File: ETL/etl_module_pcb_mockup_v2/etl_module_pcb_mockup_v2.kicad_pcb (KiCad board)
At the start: 2 copper layers, 43.1 x 56.5 mm, 10 parts, among them J1 WP7B-S050VA1-R8000, J2 WP7B-S050VA1-R8000, J3 ETROC_91pad, J4 ETROC_91pad, J5 ETROC_91pad, J6 ETROC_91pad

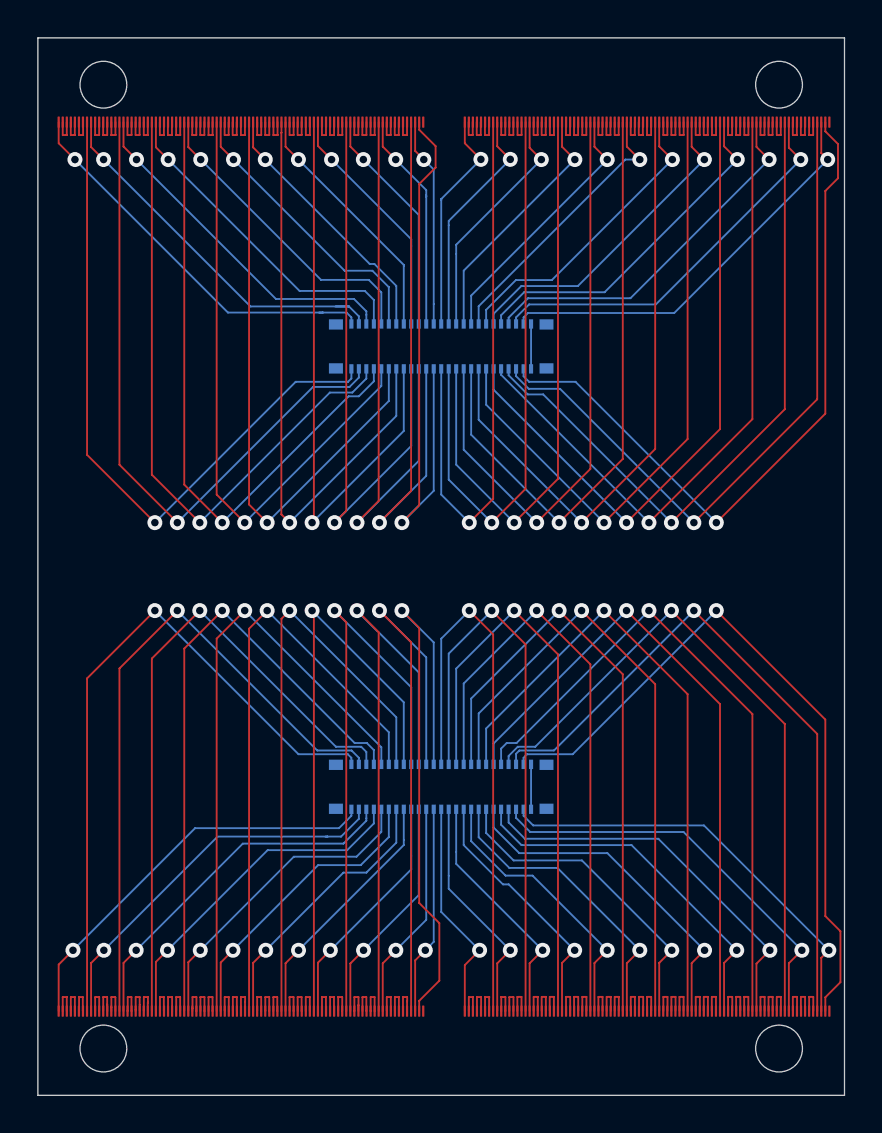
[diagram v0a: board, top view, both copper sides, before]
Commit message: Adds mockups for throughput testing
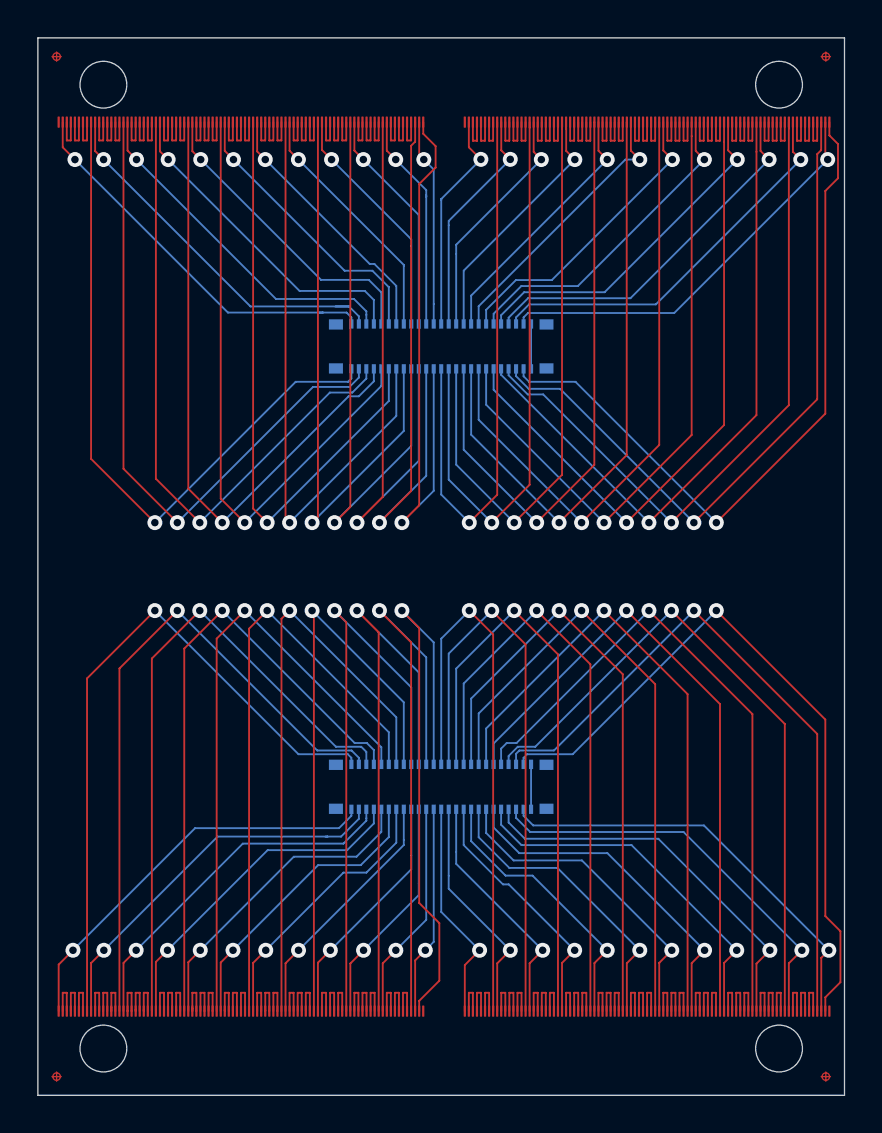
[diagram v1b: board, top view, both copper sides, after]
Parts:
- added REF**: crossed_circle_fiducial, unl_silab:crossed_circle_fiducial, F.Cu at (42.1, 55.5)
- added REF**: crossed_circle_fiducial, unl_silab:crossed_circle_fiducial, F.Cu at (1.00, 55.5)
- added REF**: crossed_circle_fiducial, unl_silab:crossed_circle_fiducial, F.Cu at (42.1, 1.00)
- added REF**: crossed_circle_fiducial, unl_silab:crossed_circle_fiducial, F.Cu at (1.00, 1.00)
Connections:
- J3 pad 1: /26_P -> Net-(J3-Pad1)
- J3 pad 10: Net-(J3-Pad10) -> /27_P
- J3 pad 11: Net-(J3-Pad10) -> Net-(J3-Pad11)
- J3 pad 12: Net-(J3-Pad12) -> Net-(J3-Pad11)
- J3 pad 13: Net-(J3-Pad12) -> Net-(J3-Pad13)
- J3 pad 14: Net-(J3-Pad14) -> Net-(J3-Pad13)
- J3 pad 15: Net-(J3-Pad14) -> Net-(J3-Pad15)
- J3 pad 16: /27_N -> Net-(J3-Pad15)
- J3 pad 17: /28_P -> /27_N
- J3 pad 18: Net-(J3-Pad18) -> /28_P
- J3 pad 19: Net-(J3-Pad18) -> Net-(J3-Pad19)
- J3 pad 2: Net-(J3-Pad2) -> /26_P
- J3 pad 20: Net-(J3-Pad20) -> Net-(J3-Pad19)
- J3 pad 21: Net-(J3-Pad20) -> Net-(J3-Pad21)
- J3 pad 22: Net-(J3-Pad22) -> Net-(J3-Pad21)
- J3 pad 23: Net-(J3-Pad22) -> Net-(J3-Pad23)
- J3 pad 24: /28_N -> Net-(J3-Pad23)
- J3 pad 25: /29_P -> /28_N
- J3 pad 26: Net-(J3-Pad26) -> /29_P
- J3 pad 27: Net-(J3-Pad26) -> Net-(J3-Pad27)
- J3 pad 28: Net-(J3-Pad28) -> Net-(J3-Pad27)
- J3 pad 29: Net-(J3-Pad28) -> Net-(J3-Pad29)
- J3 pad 3: Net-(J3-Pad2) -> Net-(J3-Pad3)
- J3 pad 30: Net-(J3-Pad30) -> Net-(J3-Pad29)
- J3 pad 31: Net-(J3-Pad30) -> Net-(J3-Pad31)
- J3 pad 32: /29_N -> Net-(J3-Pad31)
- J3 pad 33: /30_P -> /29_N
- J3 pad 34: Net-(J3-Pad34) -> /30_P
- J3 pad 35: Net-(J3-Pad34) -> Net-(J3-Pad35)
- J3 pad 36: Net-(J3-Pad36) -> Net-(J3-Pad35)
- J3 pad 37: Net-(J3-Pad36) -> Net-(J3-Pad37)
- J3 pad 38: Net-(J3-Pad38) -> Net-(J3-Pad37)
- J3 pad 39: Net-(J3-Pad38) -> Net-(J3-Pad39)
- J3 pad 4: Net-(J3-Pad4) -> Net-(J3-Pad3)
- J3 pad 40: /30_N -> Net-(J3-Pad39)
- J3 pad 41: /31_P -> /30_N
- J3 pad 42: Net-(J3-Pad42) -> /31_P
- J3 pad 43: Net-(J3-Pad42) -> Net-(J3-Pad43)
- J3 pad 44: Net-(J3-Pad44) -> Net-(J3-Pad43)
- J3 pad 45: Net-(J3-Pad44) -> Net-(J3-Pad45)
- J3 pad 46: Net-(J3-Pad46) -> Net-(J3-Pad45)
- J3 pad 47: Net-(J3-Pad46) -> Net-(J3-Pad47)
- J3 pad 48: /31_N -> Net-(J3-Pad47)
- J3 pad 49: /32_P -> /31_N
- J3 pad 5: Net-(J3-Pad4) -> Net-(J3-Pad5)
- J3 pad 50: Net-(J3-Pad50) -> /32_P
- J3 pad 51: Net-(J3-Pad50) -> Net-(J3-Pad51)
- J3 pad 52: Net-(J3-Pad52) -> Net-(J3-Pad51)
- J3 pad 53: Net-(J3-Pad52) -> Net-(J3-Pad53)
- J3 pad 54: Net-(J3-Pad54) -> Net-(J3-Pad53)
- J3 pad 55: Net-(J3-Pad54) -> Net-(J3-Pad55)
- J3 pad 56: /32_N -> Net-(J3-Pad55)
- J3 pad 57: /33_P -> /32_N
- J3 pad 58: Net-(J3-Pad58) -> /33_P
- J3 pad 59: Net-(J3-Pad58) -> Net-(J3-Pad59)
- J3 pad 6: Net-(J3-Pad6) -> Net-(J3-Pad5)
- J3 pad 60: Net-(J3-Pad60) -> Net-(J3-Pad59)
- J3 pad 61: Net-(J3-Pad60) -> Net-(J3-Pad61)
- J3 pad 62: Net-(J3-Pad62) -> Net-(J3-Pad61)
- J3 pad 63: Net-(J3-Pad62) -> Net-(J3-Pad63)
- J3 pad 64: /33_N -> Net-(J3-Pad63)
- J3 pad 65: /34_P -> /33_N
- J3 pad 66: Net-(J3-Pad66) -> /34_P
- J3 pad 67: Net-(J3-Pad66) -> Net-(J3-Pad67)
- J3 pad 68: Net-(J3-Pad68) -> Net-(J3-Pad67)
- J3 pad 69: Net-(J3-Pad68) -> Net-(J3-Pad69)
- J3 pad 7: Net-(J3-Pad6) -> Net-(J3-Pad7)
- J3 pad 70: Net-(J3-Pad70) -> Net-(J3-Pad69)
- J3 pad 71: Net-(J3-Pad70) -> Net-(J3-Pad71)
- J3 pad 72: /34_N -> Net-(J3-Pad71)
- J3 pad 73: /35_P -> /34_N
- J3 pad 74: Net-(J3-Pad74) -> /35_P
- J3 pad 75: Net-(J3-Pad74) -> Net-(J3-Pad75)
- J3 pad 76: Net-(J3-Pad76) -> Net-(J3-Pad75)
- J3 pad 77: Net-(J3-Pad76) -> Net-(J3-Pad77)
- J3 pad 78: Net-(J3-Pad78) -> Net-(J3-Pad77)
- J3 pad 79: Net-(J3-Pad78) -> Net-(J3-Pad79)
- J3 pad 8: /26_N -> Net-(J3-Pad7)
- J3 pad 80: /35_N -> Net-(J3-Pad79)
- J3 pad 81: /36_P -> /35_N
- J3 pad 82: Net-(J3-Pad82) -> /36_P
- J3 pad 83: Net-(J3-Pad82) -> Net-(J3-Pad83)
- J3 pad 84: Net-(J3-Pad84) -> Net-(J3-Pad83)
- J3 pad 85: Net-(J3-Pad84) -> Net-(J3-Pad85)
- J3 pad 86: Net-(J3-Pad86) -> Net-(J3-Pad85)
- J3 pad 87: Net-(J3-Pad86) -> Net-(J3-Pad87)
- J3 pad 88: /36_N -> Net-(J3-Pad87)
- J3 pad 89: /37_P -> /36_N
- J3 pad 9: /27_P -> /26_N
- J3 pad 90: /37_N -> /37_P
- J3 pad 91: Net-(J3-Pad91) -> /37_N
- J4 pad 1: /38_P -> Net-(J4-Pad1)
- J4 pad 10: Net-(J4-Pad10) -> /39_P
- J4 pad 11: Net-(J4-Pad10) -> Net-(J4-Pad11)
- J4 pad 12: Net-(J4-Pad12) -> Net-(J4-Pad11)
- J4 pad 13: Net-(J4-Pad12) -> Net-(J4-Pad13)
- J4 pad 14: Net-(J4-Pad14) -> Net-(J4-Pad13)
- J4 pad 15: Net-(J4-Pad14) -> Net-(J4-Pad15)
- J4 pad 16: /39_N -> Net-(J4-Pad15)
- J4 pad 17: /40_P -> /39_N
- J4 pad 18: Net-(J4-Pad18) -> /40_P
- J4 pad 19: Net-(J4-Pad18) -> Net-(J4-Pad19)
- J4 pad 2: Net-(J4-Pad2) -> /38_P
- J4 pad 20: Net-(J4-Pad20) -> Net-(J4-Pad19)
- J4 pad 21: Net-(J4-Pad20) -> Net-(J4-Pad21)
- J4 pad 22: Net-(J4-Pad22) -> Net-(J4-Pad21)
- J4 pad 23: Net-(J4-Pad22) -> Net-(J4-Pad23)
- J4 pad 24: /40_N -> Net-(J4-Pad23)
- J4 pad 25: /41_P -> /40_N
- J4 pad 26: Net-(J4-Pad26) -> /41_P
- J4 pad 27: Net-(J4-Pad26) -> Net-(J4-Pad27)
- J4 pad 28: Net-(J4-Pad28) -> Net-(J4-Pad27)
- J4 pad 29: Net-(J4-Pad28) -> Net-(J4-Pad29)
- J4 pad 3: Net-(J4-Pad2) -> Net-(J4-Pad3)
- J4 pad 30: Net-(J4-Pad30) -> Net-(J4-Pad29)
- J4 pad 31: Net-(J4-Pad30) -> Net-(J4-Pad31)
- J4 pad 32: /41_N -> Net-(J4-Pad31)
- J4 pad 33: /42_P -> /41_N
- J4 pad 34: Net-(J4-Pad34) -> /42_P
- J4 pad 35: Net-(J4-Pad34) -> Net-(J4-Pad35)
- J4 pad 36: Net-(J4-Pad36) -> Net-(J4-Pad35)
- J4 pad 37: Net-(J4-Pad36) -> Net-(J4-Pad37)
- J4 pad 38: Net-(J4-Pad38) -> Net-(J4-Pad37)
- J4 pad 39: Net-(J4-Pad38) -> Net-(J4-Pad39)
- J4 pad 4: Net-(J4-Pad4) -> Net-(J4-Pad3)
- J4 pad 40: /42_N -> Net-(J4-Pad39)
- J4 pad 41: /43_P -> /42_N
- J4 pad 42: Net-(J4-Pad42) -> /43_P
- J4 pad 43: Net-(J4-Pad42) -> Net-(J4-Pad43)
- J4 pad 44: Net-(J4-Pad44) -> Net-(J4-Pad43)
- J4 pad 45: Net-(J4-Pad44) -> Net-(J4-Pad45)
- J4 pad 46: Net-(J4-Pad46) -> Net-(J4-Pad45)
- J4 pad 47: Net-(J4-Pad46) -> Net-(J4-Pad47)
- J4 pad 48: /43_N -> Net-(J4-Pad47)
- J4 pad 49: /44_P -> /43_N
- J4 pad 5: Net-(J4-Pad4) -> Net-(J4-Pad5)
- J4 pad 50: Net-(J4-Pad50) -> /44_P
- J4 pad 51: Net-(J4-Pad50) -> Net-(J4-Pad51)
- J4 pad 52: Net-(J4-Pad52) -> Net-(J4-Pad51)
- J4 pad 53: Net-(J4-Pad52) -> Net-(J4-Pad53)
- J4 pad 54: Net-(J4-Pad54) -> Net-(J4-Pad53)
- J4 pad 55: Net-(J4-Pad54) -> Net-(J4-Pad55)
- J4 pad 56: /44_N -> Net-(J4-Pad55)
- J4 pad 57: /45_P -> /44_N
- J4 pad 58: Net-(J4-Pad58) -> /45_P
- J4 pad 59: Net-(J4-Pad58) -> Net-(J4-Pad59)
- J4 pad 6: Net-(J4-Pad6) -> Net-(J4-Pad5)
- J4 pad 60: Net-(J4-Pad60) -> Net-(J4-Pad59)
- J4 pad 61: Net-(J4-Pad60) -> Net-(J4-Pad61)
- J4 pad 62: Net-(J4-Pad62) -> Net-(J4-Pad61)
- J4 pad 63: Net-(J4-Pad62) -> Net-(J4-Pad63)
- J4 pad 64: /45_N -> Net-(J4-Pad63)
- J4 pad 65: /46_P -> /45_N
- J4 pad 66: Net-(J4-Pad66) -> /46_P
- J4 pad 67: Net-(J4-Pad66) -> Net-(J4-Pad67)
- J4 pad 68: Net-(J4-Pad68) -> Net-(J4-Pad67)
- J4 pad 69: Net-(J4-Pad68) -> Net-(J4-Pad69)
- J4 pad 7: Net-(J4-Pad6) -> Net-(J4-Pad7)
- J4 pad 70: Net-(J4-Pad70) -> Net-(J4-Pad69)
- J4 pad 71: Net-(J4-Pad70) -> Net-(J4-Pad71)
- J4 pad 72: /46_N -> Net-(J4-Pad71)
- J4 pad 73: /47_P -> /46_N
- J4 pad 74: Net-(J4-Pad74) -> /47_P
- J4 pad 75: Net-(J4-Pad74) -> Net-(J4-Pad75)
- J4 pad 76: Net-(J4-Pad76) -> Net-(J4-Pad75)
- J4 pad 77: Net-(J4-Pad76) -> Net-(J4-Pad77)
- J4 pad 78: Net-(J4-Pad78) -> Net-(J4-Pad77)
- J4 pad 79: Net-(J4-Pad78) -> Net-(J4-Pad79)
- J4 pad 8: /38_N -> Net-(J4-Pad7)
- J4 pad 80: /47_N -> Net-(J4-Pad79)
- J4 pad 81: /48_P -> /47_N
- J4 pad 82: Net-(J4-Pad82) -> /48_P
- J4 pad 83: Net-(J4-Pad82) -> Net-(J4-Pad83)
- J4 pad 84: Net-(J4-Pad84) -> Net-(J4-Pad83)
- J4 pad 85: Net-(J4-Pad84) -> Net-(J4-Pad85)
- J4 pad 86: Net-(J4-Pad86) -> Net-(J4-Pad85)
- J4 pad 87: Net-(J4-Pad86) -> Net-(J4-Pad87)
- J4 pad 88: /48_N -> Net-(J4-Pad87)
- J4 pad 89: /49_P -> /48_N
- J4 pad 9: /39_P -> /38_N
- J4 pad 90: /49_N -> /49_P
- J4 pad 91: Net-(J4-Pad91) -> /49_N
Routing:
- net Net-(J4-Pad3): track 0.00 -> 2.20 mm
- net Net-(J4-Pad85): track 0.00 -> 2.20 mm
- net Net-(J4-Pad79): track 0.00 -> 2.20 mm
- net Net-(J4-Pad67): track 0.00 -> 2.20 mm
- net Net-(J4-Pad63): track 0.00 -> 2.20 mm
- net Net-(J4-Pad51): track 0.00 -> 2.20 mm
- net Net-(J4-Pad47): track 0.00 -> 2.20 mm
- net Net-(J4-Pad7): track 0.00 -> 2.20 mm
- net Net-(J4-Pad39): track 0.00 -> 2.20 mm
- net Net-(J4-Pad37): track 0.00 -> 2.20 mm
- net Net-(J4-Pad31): track 0.00 -> 2.20 mm
- net Net-(J4-Pad29): track 0.00 -> 2.20 mm
- net Net-(J4-Pad27): track 0.00 -> 2.20 mm
- net Net-(J4-Pad23): track 0.00 -> 2.20 mm
- net Net-(J4-Pad19): track 0.00 -> 2.20 mm
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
